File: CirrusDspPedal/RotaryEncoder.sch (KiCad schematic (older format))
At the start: 3 parts, among them SW5 Rotary_Encoder_Switch

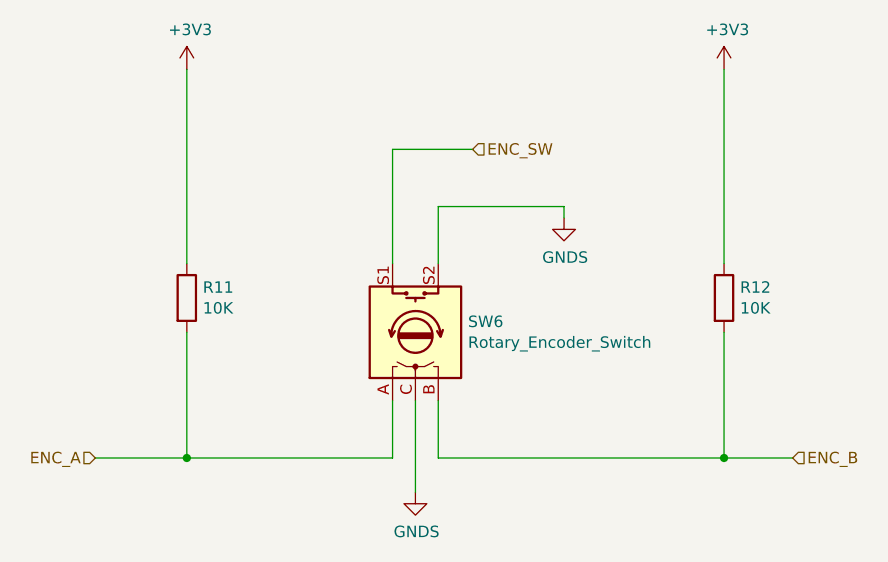
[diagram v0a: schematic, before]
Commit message: updated revb
- Moved THT components to improve UX layout
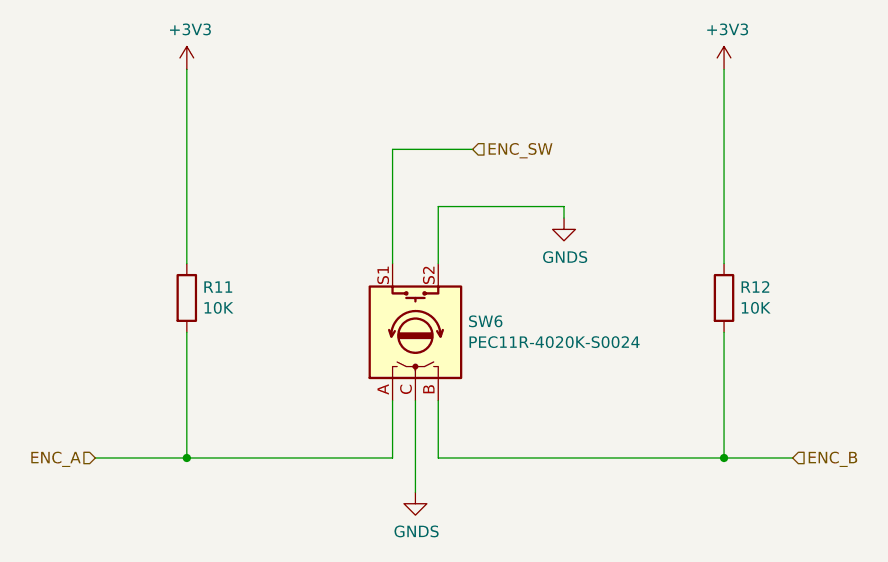
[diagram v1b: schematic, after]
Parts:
- SW5: value Rotary_Encoder_Switch -> PEC11R-4020K-S0024
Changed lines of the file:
@@
 AR Path="/5F898CA5/5FAC8ACD/5FAC4008" Ref="SW6"  Part="1"
 F 0 "SW6" V 5746 3020 50  0000 R CNN
-F 1 "Rotary_Encoder_Switch" V 5655 3020 50  0000 R CNN
+F 1 "PEC11R-4020K-S0024" V 5655 3020 50  0000 R CNN
 F 2 "Rotary_Encoder:RotaryEncoder_Alps_EC11E-Switch_Vertical_H20mm" H 5550 3410 50  0001 C CNN
-F 3 "~" H 5700 3510 50  0001 C CNN
+F 3 "https://docs.rs-online.com/6e29/0900766b80fa5804.pdf" H 5700 3510 50  0001 C CNN
 	1    5700 3250
 	0    -1   -1   0
